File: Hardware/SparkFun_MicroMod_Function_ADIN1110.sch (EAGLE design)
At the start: 78 parts, among them J1 T1_INDUSTRIAL, J2 MICROMOD_FUNCTION_STANDARD, Q1 220mA/50V/3.5Ω, Q2 20V/4.2A/52mΩ/1.4W, T1 WE-STST, U1 ADIN1110, U2 EEPROM, U3 3.3V, U4 WE-TVS, Y1 25MHz

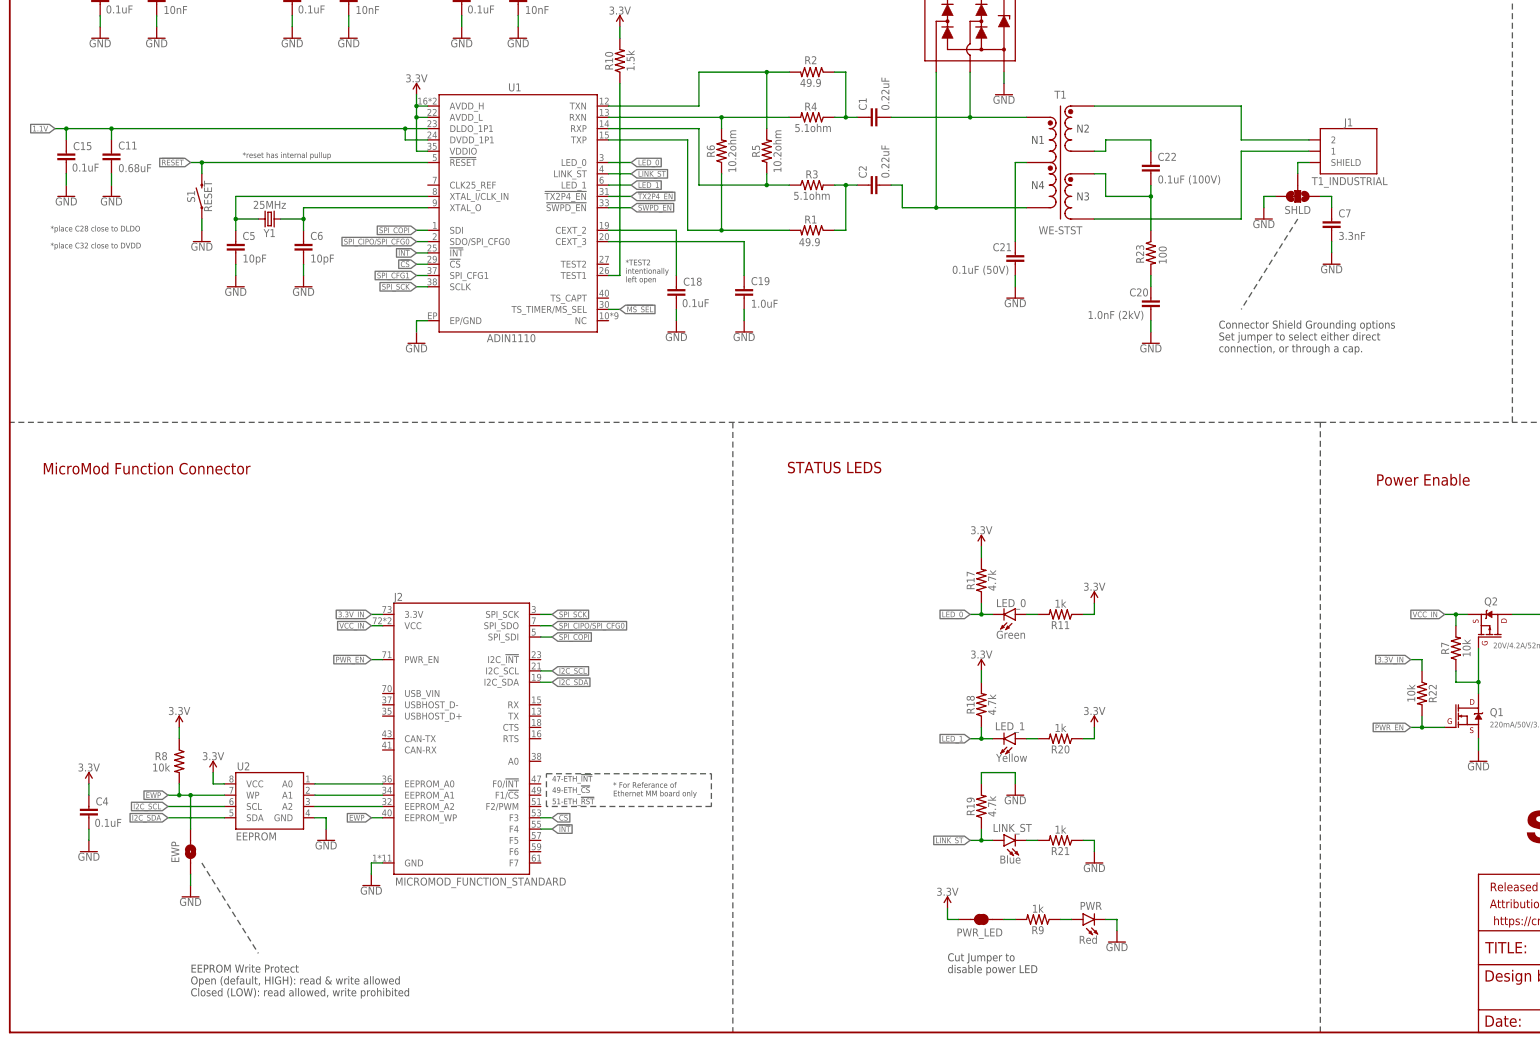
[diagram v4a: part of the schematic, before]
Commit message: Prototype Design Review Changes
-Moved LEDs to upper edge.
-Backed off GND pour from connector for better isolation
-added jumpers to disable each LED if desired
-Schematic symbols cleanup and note corrections
-moved 3.3V testpoint to match other Ethernet MM board.
-tightened FP drills on T1 connector
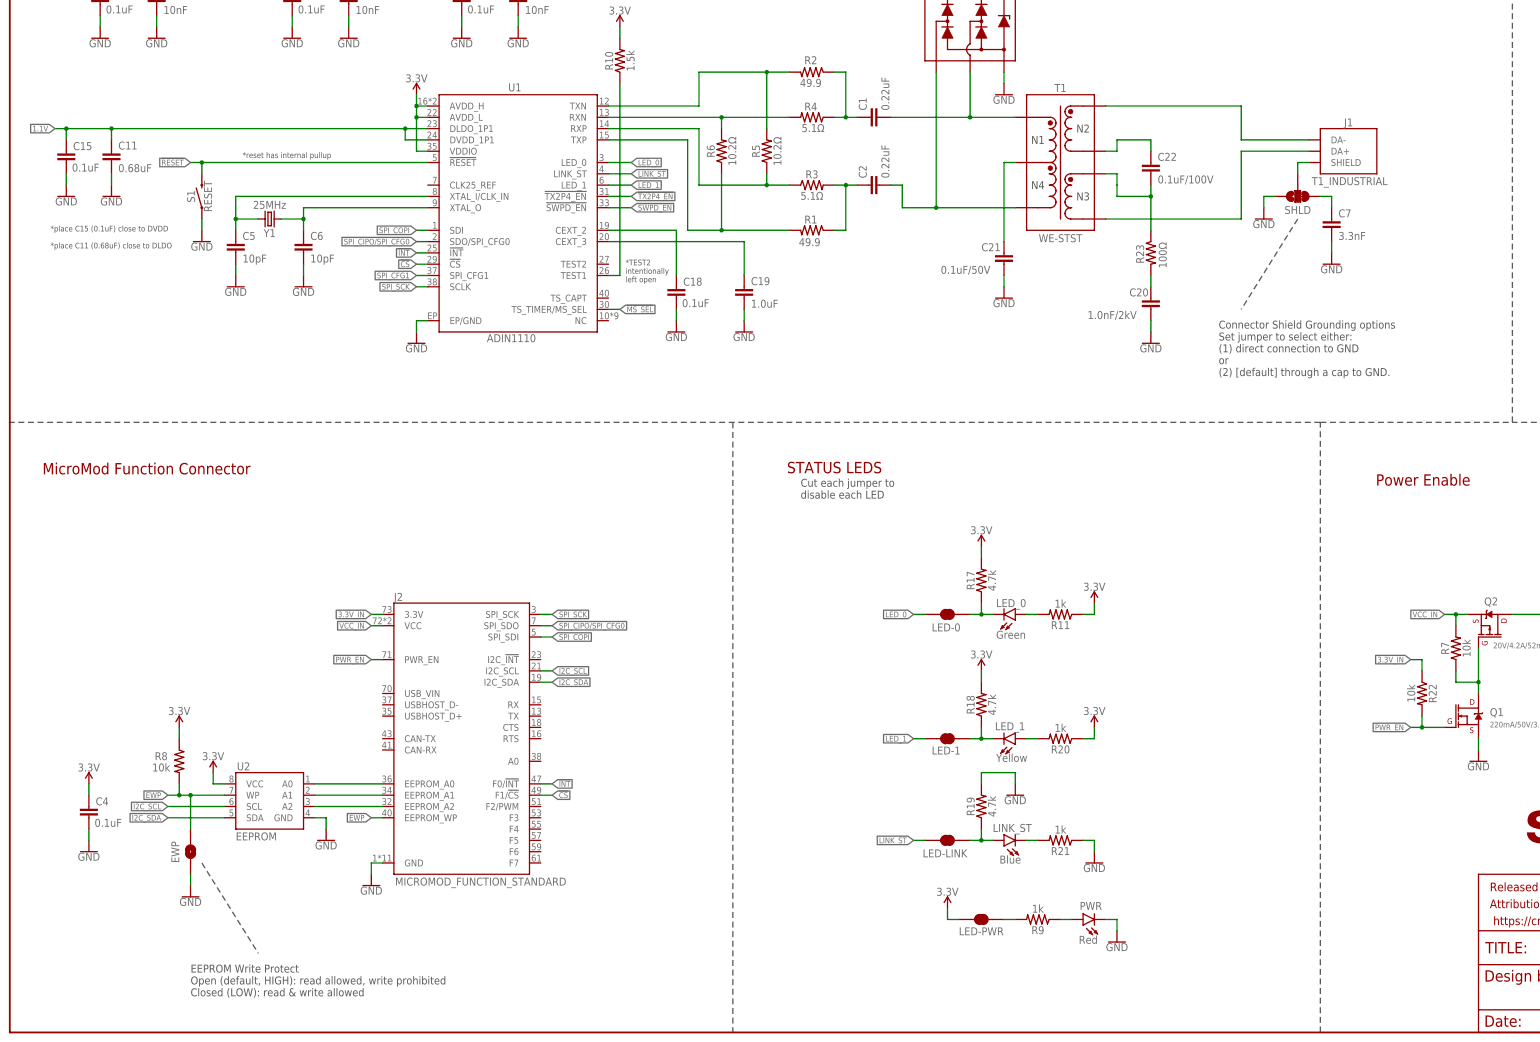
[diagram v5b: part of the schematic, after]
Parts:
- added LED-0, LED-1, LED-LINK: JUMPER-SMT_2_NC_TRACE_SILK, SparkFun-Jumpers:JUMPER-SMT_2_NC_TRACE_SILK
- C20: value 1.0nF (2kV) -> 1.0nF/2kV
- C21: value 0.1uF (50V) -> 0.1uF/50V
- C22: value 0.1uF (100V) -> 0.1uF/100V
- R23: value 100 -> 100Ω
- R3, R4: value 5.1ohm -> 5.1Ω
- R5, R6: value 10.2ohm -> 10.2Ω
- renumbered PWR_LED to LED-PWR
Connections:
- new net DA+: J1.DA+, T1.7
- new net DA-: J1.DA-, T1.6
- new net N$9: LED-0.1, LED_0.C, R17.1
- net !CS!: now also J2.F1/!CS!; no longer J2.F3
- net !INT!: now also J2.F0/!INT!; no longer J2.F4
- net GND: now also SHLD.1; no longer SHLD.3
- net LED_0: now also LED-0.2; no longer LED_0.C, R17.1
- net LED_1: now also LED-1.2; no longer LED_1.C, R18.1
- net LINK_ST: now also LED-LINK.2; no longer LINK_ST.A, R19.1
- net N$41: now also SHLD.3; no longer SHLD.1
- net N$5: now also LED-LINK.1, LINK_ST.A, R19.1; no longer J1.2, T1.6
- net N$6: now also LED-1.1, LED_1.C, R18.1; no longer J1.1, T1.7
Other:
- note added: "*place C15 (0.1uF) close to DVDD *place C11 (0.68uF) close to DLDO"
- note added: "Connector Shield Grounding options Set jumper to select either: (1) direct connection to GND or (2) [default] through a cap to GND."
- note added: "Cut each jumper to disable each LED"
- note added: "EEPROM Write Protect Open (default, HIGH): read allowed, write prohibited Closed (LOW): read & write allowed"
- note removed: "* For Referance of Ethernet MM board only"
- note removed: "*place C28 close to DLDO *place C32 close to DVDD"
- note removed: "47-ETH_!INT!"
- note removed: "49-ETH_!CS!"
- note removed: "51-ETH_!RST!"
- note removed: "Connector Shield Grounding options Set jumper to select either direct connection, or through a cap."
- note removed: "Cut Jumper to disable power LED"
- note removed: "EEPROM Write Protect Open (default, HIGH): read & write allowed Closed (LOW): read allowed, write prohibited"
- moved on the sheet: C21
